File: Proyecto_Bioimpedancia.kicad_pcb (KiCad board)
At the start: 2 copper layers, 100 x 100 mm, 69 parts, among them J1 Jumper, J2 Jumper, J3 Jumper_Calibration, J4 Jumper, J5 Jumper, J6 Jumper, P1 SD_LAPIZ, P10 RS-232, P11 SOURCE_2, P12 RESET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

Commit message: PCB version final
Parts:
- added C14: 0,1uF, Capacitors_SMD:C_0805_HandSoldering, F.Cu at (165.6, 53.1)
- P10: value RS-232 -> UNIVERSAL_PINS; footprint Socket_Strips:Socket_Strip_Straight_1x03_Pitch2.54mm -> Huellas:Universal_Path_80_Pins
- P6: value I2C_1 -> I2C; footprint Socket_Strips:Socket_Strip_Straight_1x02_Pitch2.54mm -> Socket_Strips:Socket_Strip_Straight_2x04_Pitch2.54mm
- P7: value I2C_2 -> CONN_01X04; footprint Socket_Strips:Socket_Strip_Straight_1x02_Pitch2.54mm -> Socket_Strips:Socket_Strip_Straight_1x04_Pitch2.54mm
- moved P10 75.2 mm to (154.5, 124.0), turned to 0 degrees
- moved P7 73.6 mm to (158.0, 48.8), turned to 90 degrees
- moved P12 3.11 mm to (170.8, 48.7)
- moved P6 1.89 mm to (92.3, 87.4), turned to 180 degrees
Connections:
- P6 pad 1: /SDA_R -> /SCL_R
- P6 pad 2: /SCL_R -> /SDA_R
- P7 pad 1: /SDA_R -> /AGND
- P7 pad 2: /SCL_R -> /TXD
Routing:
- net /SDA_R: track 47.7 -> 32.7 mm
- net /SCL_R: track 56.0 -> 43.7 mm, vias 3 -> 2
- net Net-(C14-Pad1): track 0.00 -> 3.03 mm
- net /RXD: track 79.1 -> 76.4 mm
- net /RESET: track 89.0 -> 90.4 mm
- net /AGND: track 172.6 -> 173.6 mm, vias 59 -> 95
- net /SCK: track 21.1 -> 21.9 mm
- net (no net): vias 0 -> 2
- added copper zone on F.Cu, net Net-(C11-Pad2)
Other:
- board text added: "5V"
- board text added: "BIO_OUT1"
- board text added: "BIO_OUT2"
- board text added: "ENC_1"
- board text added: "ENC_2"
- board text added: "GND"
- board text added: "GPIO"
- board text added: "MISO"
- board text added: "MOSI"
- board text added: "RESET"
- board text added: "RX"
- board text added: "RX_V"
- board text added: "SCK"
- board text added: "SCL"
- board text added: "SDA"
- board text added: "TX"
- board text added: "TX_V"
- board text added: "UNIVERSAL_PINS"
- board text added: "V_FUENTE"
- board text added: "~SS"

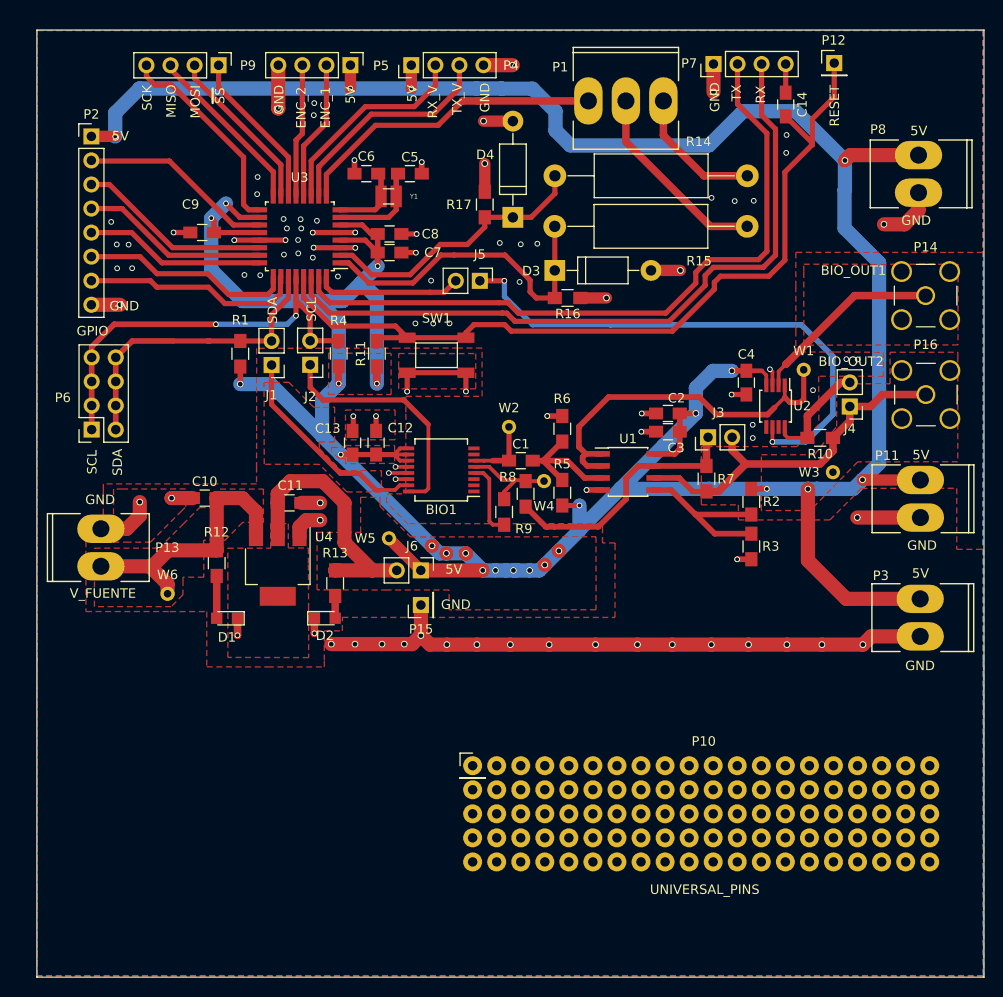
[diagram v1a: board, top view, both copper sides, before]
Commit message: Regleta Universal Añadida
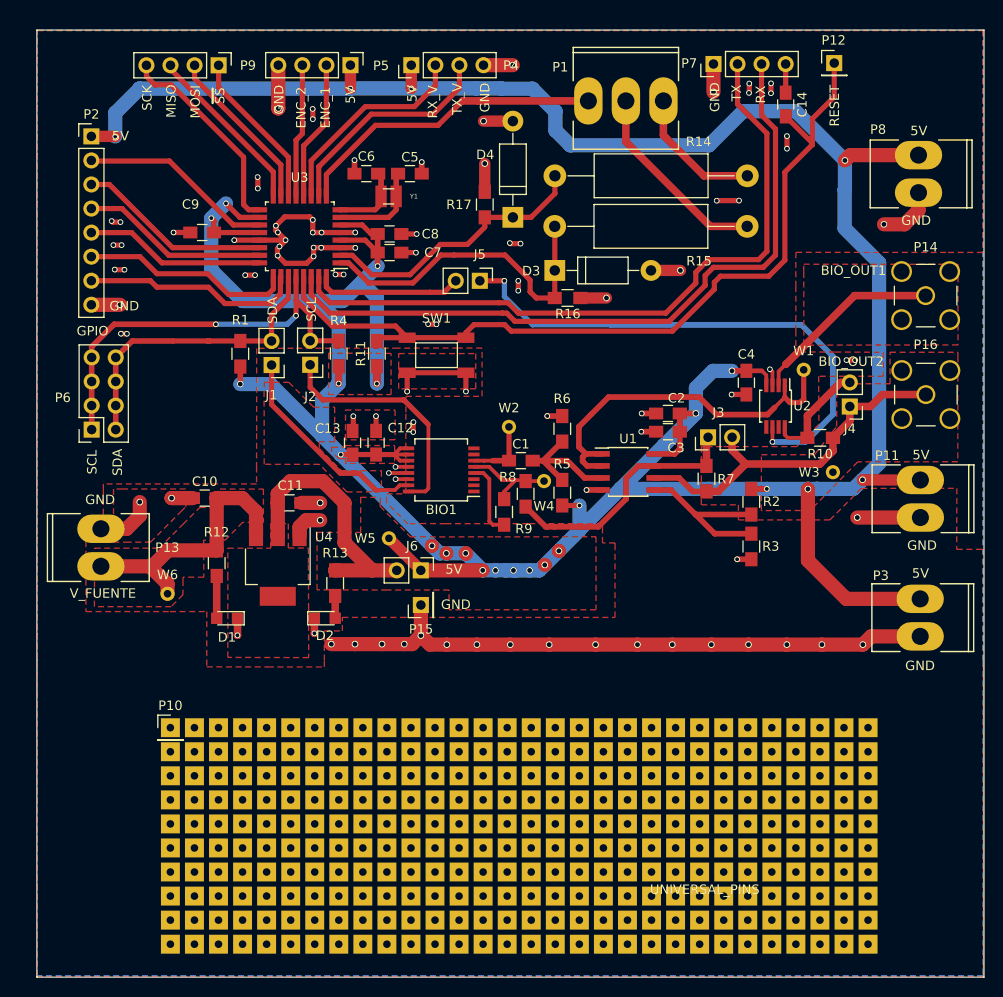
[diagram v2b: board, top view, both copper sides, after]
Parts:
- P10: footprint Huellas:Universal_Path_80_Pins -> Huellas:Universal_Path_300_Pins
- moved P10 54.1 mm to (100.7, 118.9)
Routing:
- net /AGND: track 173.6 -> 207.3 mm, vias 95 -> 100
- net (no net): vias 2 -> 0

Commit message: Gerber generado
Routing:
- net (no net): track 0.00 -> 18.6 mm, vias 0 -> 34
- net /AGND: track 207.3 -> 188.7 mm, vias 100 -> 66

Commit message: Version para placa
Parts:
- added P17: TOR_1, Mounting_Holes:MountingHole_3.2mm_M3_Pad_Via, F.Cu at (91.6, 50.2)
- added P18: TOR_2, Mounting_Holes:MountingHole_3.2mm_M3_Pad_Via, F.Cu at (181.6, 50.2)
- added P19: TOR_3, Mounting_Holes:MountingHole_3.2mm_M3_Pad_Via, F.Cu at (91.6, 140.2)
- added P20: TOR_4, Mounting_Holes:MountingHole_3.2mm_M3_Pad_Via, F.Cu at (181.6, 140.2)
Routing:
- net /AGND: track 188.7 -> 372.8 mm, vias 66 -> 117
- net (no net): track 18.6 -> 0.00 mm, vias 34 -> 0
- net /5V: track 389.5 -> 394.6 mm, vias 26 -> 27
- net /SCL_R: track 43.7 -> 43.2 mm

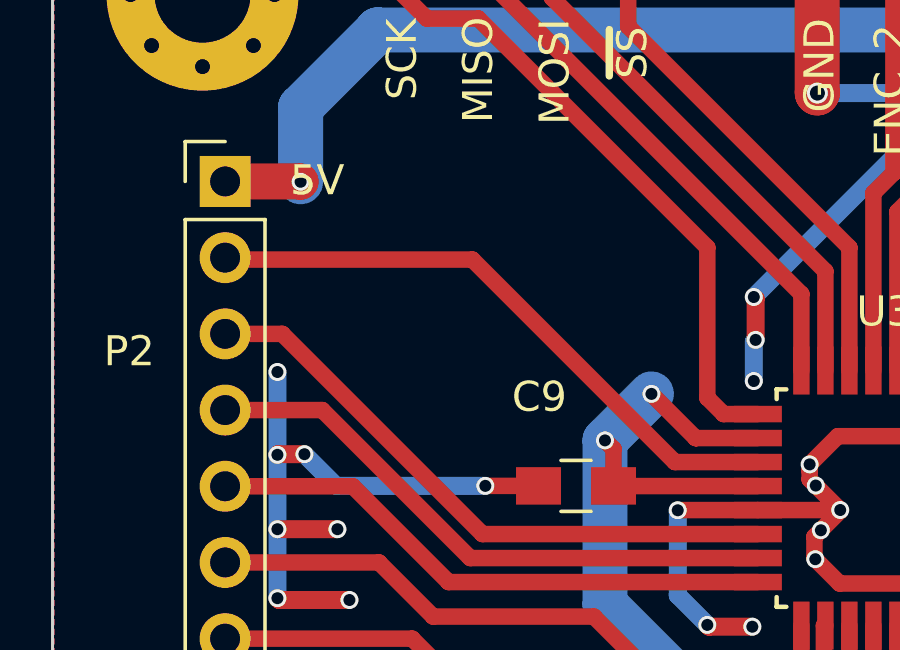
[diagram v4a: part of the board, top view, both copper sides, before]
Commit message: Led Prueba Blink Añadido
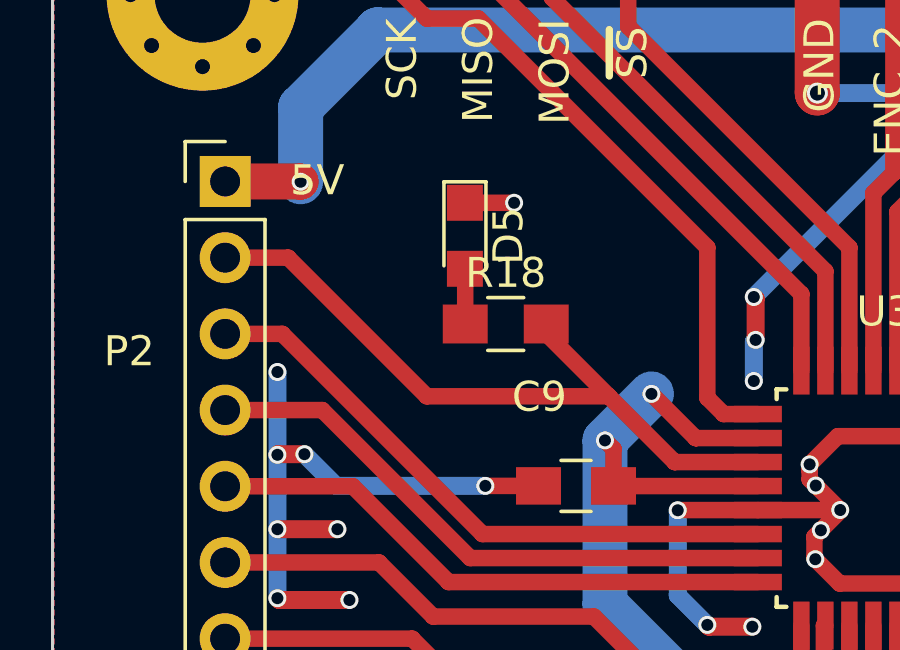
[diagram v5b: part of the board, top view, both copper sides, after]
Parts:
- added D5: Led_Small_Reg, LEDs:LED_0805, F.Cu at (100.3, 58.2)
- added R18: 1K, Resistors_SMD:R_0805_HandSoldering, F.Cu at (101.7, 61.2)
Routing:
- net /REG2_1: track 20.6 -> 23.9 mm
- net Net-(D5-Pad2): track 0.00 -> 1.84 mm
- net /AGND: track 372.8 -> 374.4 mm, vias 117 -> 118
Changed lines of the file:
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@@
 (kicad_pcb (version 4) (host pcbnew 4.0.2-stable)
   (general
-    (links 154)
+    (links 157)
     (no_connects 0)
     (area 86.513199 43.591666 186.613201 145.487)
     (thickness 1.6)
     (drawings 42)
-    (tracks 932)
+    (tracks 940)
     (zones 0)
-    (modules 74)
-    (nets 54)
+    (modules 76)
+    (nets 55)
   )
   (page A4)
@@
   )
   (setup
-    (last_trace_width 0.6)
+    (last_trace_width 0.55)
     (user_trace_width 0.4)
     (user_trace_width 0.5)
@@
   (net 52 "Net-(P19-Pad1)")
   (net 53 "Net-(P20-Pad1)")
+  (net 54 "Net-(D5-Pad2)")
   (net_class Default "Esta es la clase de red por defecto."
     (clearance 0.2)
@@
     (add_net "Net-(D1-Pad2)")
     (add_net "Net-(D2-Pad2)")
+    (add_net "Net-(D5-Pad2)")
     (add_net "Net-(J4-Pad2)")
     (add_net "Net-(J5-Pad2)")
@@
     (pad "" thru_hole circle (at 1.697056 -1.697056) (size 0.8 0.8) (drill 0.5) (layers *.Cu *.Mask))
   )
+  (module LEDs:LED_0805 (layer F.Cu)
+    (at 100.31 58.25 270)
+    (descr "LED 0805 smd package")
+    (tags "LED led 0805 SMD smd SMT smt smdled SMDLED smtled SMTLED")
+    (attr smd)
+    (fp_text reference D5 (at 0 -1.45 270) (layer F.SilkS)
+      (effects (font (size 1 1) (thickness 0.15)))
+    )
+    (fp_text value Led_Small_Reg (at 0 1.55 270) (layer F.Fab)
+      (effects (font (size 1 1) (thickness 0.15)))
+    )
+    (fp_line (start -1.8 -0.7) (end -1.8 0.7) (layer F.SilkS) (width 0.12))
+    (fp_line (start -0.4 -0.4) (end -0.4 0.4) (layer F.Fab) (width 0.1))
+    (fp_line (start -0.4 0) (end 0.2 -0.4) (layer F.Fab) (width 0.1))
+    (fp_line (start 0.2 0.4) (end -0.4 0) (layer F.Fab) (width 0.1))
+    (fp_line (start 0.2 -0.4) (end 0.2 0.4) (layer F.Fab) (width 0.1))
+    (fp_line (start 1 0.6) (end -1 0.6) (layer F.Fab) (width 0.1))
+    (fp_line (start 1 -0.6) (end 1 0.6) (layer F.Fab) (width 0.1))
+    (fp_line (start -1 -0.6) (end 1 -0.6) (layer F.Fab) (width 0.1))
+    (fp_line (start -1 0.6) (end -1 -0.6) (layer F.Fab) (width 0.1))
+    (fp_line (start -1.8 0.7) (end 1 0.7) (layer F.SilkS) (width 0.12))
+    (fp_line (start -1.8 -0.7) (end 1 -0.7) (layer F.SilkS) (width 0.12))
+    (fp_line (start 1.95 -0.85) (end 1.95 0.85) (layer F.CrtYd) (width 0.05))
+    (fp_line (start 1.95 0.85) (end -1.95 0.85) (layer F.CrtYd) (width 0.05))
+    (fp_line (start -1.95 0.85) (end -1.95 -0.85) (layer F.CrtYd) (width 0.05))
+    (fp_line (start -1.95 -0.85) (end 1.95 -0.85) (layer F.CrtYd) (width 0.05))
+    (fp_text user %R (at 0 -1.25 270) (layer F.Fab)
+      (effects (font (size 0.4 0.4) (thickness 0.1)))
+    )
+    (pad 2 smd rect (at 1.1 0 90) (size 1.2 1.2) (layers F.Cu F.Paste F.Mask)
+      (net 54 "Net-(D5-Pad2)"))
+    (pad 1 smd rect (at -1.1 0 90) (size 1.2 1.2) (layers F.Cu F.Paste F.Mask)
+      (net 5 /AGND))
+    (model ${KISYS3DMOD}/LEDs.3dshapes/LED_0805.wrl
+      (at (xyz 0 0 0))
+      (scale (xyz 1 1 1))
+      (rotate (xyz 0 0 180))
+    )
+  )
+  (module Resistors_SMD:R_0805_HandSoldering (layer F.Cu)
+    (at 101.67 61.19)
+    (descr "Resistor SMD 0805, hand soldering")
+    (tags "resistor 0805")
+    (attr smd)
+    (fp_text reference R18 (at 0 -1.7) (layer F.SilkS)
+      (effects (font (size 1 1) (thickness 0.15)))
+    )
+    (fp_text value 1K (at 0 1.75) (layer F.Fab)
+      (effects (font (size 1 1) (thickness 0.15)))
+    )
+    (fp_text user %R (at 0 0) (layer F.Fab)
+      (effects (font (size 0.5 0.5) (thickness 0.075)))
+    )
+    (fp_line (start -1 0.62) (end -1 -0.62) (layer F.Fab) (width 0.1))
+    (fp_line (start 1 0.62) (end -1 0.62) (layer F.Fab) (width 0.1))
+    (fp_line (start 1 -0.62) (end 1 0.62) (layer F.Fab) (width 0.1))
+    (fp_line (start -1 -0.62) (end 1 -0.62) (layer F.Fab) (width 0.1))
+    (fp_line (start 0.6 0.88) (end -0.6 0.88) (layer F.SilkS) (width 0.12))
+    (fp_line (start -0.6 -0.88) (end 0.6 -0.88) (layer F.SilkS) (width 0.12))
+    (fp_line (start -2.35 -0.9) (end 2.35 -0.9) (layer F.CrtYd) (width 0.05))
+    (fp_line (start -2.35 -0.9) (end -2.35 0.9) (layer F.CrtYd) (width 0.05))
+    (fp_line (start 2.35 0.9) (end 2.35 -0.9) (layer F.CrtYd) (width 0.05))
+    (fp_line (start 2.35 0.9) (end -2.35 0.9) (layer F.CrtYd) (width 0.05))
+    (pad 1 smd rect (at -1.35 0) (size 1.5 1.3) (layers F.Cu F.Paste F.Mask)
+      (net 54 "Net-(D5-Pad2)"))
+    (pad 2 smd rect (at 1.35 0) (size 1.5 1.3) (layers F.Cu F.Paste F.Mask)
+      (net 24 /REG2_1))
+    (model ${KISYS3DMOD}/Resistors_SMD.3dshapes/R_0805.wrl
+      (at (xyz 0 0 0))
+      (scale (xyz 1 1 1))
+      (rotate (xyz 0 0 0))
+    )
+  )
   (gr_text UNIVERSAL_PINS (at 136.11 116.37) (layer F.SilkS)
     (effects (font (size 1 1) (thickness 0.25)))
@@
   (segment (start 132.70552 90.67836) (end 133.76438 90.67836) (width 0.4) (layer F.Cu) (net 3))
   (segment (start 133.76438 90.67836) (end 133.7691 90.68308) (width 0.4) (layer F.Cu) (net 3))
+  (segment (start 100.31 57.15) (end 101.95 57.15) (width 0.55) (layer F.Cu) (net 5))
+  (via (at 101.95 57.15) (size 0.6) (drill 0.4) (layers F.Cu B.Cu) (net 5))
   (segment (start 121.31 76.32) (end 120.86 76.77) (width 0.6) (layer B.Cu) (net 5))
   (via (at 119.87 77.56) (size 0.6) (drill 0.4) (layers F.Cu B.Cu) (net 5))
@@
   (segment (start 119.4749 69.7925) (end 121.59996 71.91756) (width 0.55) (layer F.Cu) (net 23))
   (segment (start 121.59996 71.91756) (end 121.63044 71.94804) (width 0.55) (layer F.Cu) (net 23))
+  (segment (start 103.02 61.19) (end 103.02 61.51) (width 0.55) (layer F.Cu) (net 24))
+  (segment (start 103.02 61.51) (end 105.11 63.6) (width 0.55) (layer F.Cu) (net 24))
+  (segment (start 107.3088 65.7925) (end 107.3025 65.7925) (width 0.55) (layer F.Cu) (net 24))
   (segment (start 110.0754 65.7925) (end 107.3088 65.7925) (width 0.55) (layer F.Cu) (net 24))
-  (segment (start 100.5586 59.0423) (end 92.3798 59.0423) (width 0.55) (layer F.Cu) (net 24))
-  (segment (start 107.3088 65.7925) (end 100.5586 59.0423) (width 0.55) (layer F.Cu) (net 24))
-  (segment (start 92.3798 59.0423) (end 92.3163 58.9788) (width 0.55) (layer F.Cu) (net 24))
+  (segment (start 94.4188 58.9788) (end 92.3163 58.9788) (width 0.55) (layer F.Cu) (net 24))
+  (segment (start 99.04 63.6) (end 94.4188 58.9788) (width 0.55) (layer F.Cu) (net 24))
+  (segment (start 105.11 63.6) (end 99.04 63.6) (width 0.55) (layer F.Cu) (net 24))
+  (segment (start 107.3025 65.7925) (end 105.11 63.6) (width 0.55) (layer F.Cu) (net 24))
   (segment (start 110.0754 68.1925) (end 100.8953 68.1925) (width 0.55) (layer F.Cu) (net 25))
   (segment (start 94.2216 61.5188) (end 92.3163 61.5188) (width 0.55) (layer F.Cu) (net 25))
@@
   (segment (start 165.625 51.825) (end 165.625 48.805) (width 0.55) (layer F.Cu) (net 48))
   (segment (start 165.625 48.805) (end 165.62 48.8) (width 0.55) (layer F.Cu) (net 48))
+  (segment (start 100.32 61.19) (end 100.32 59.36) (width 0.55) (layer F.Cu) (net 54))
+  (segment (start 100.32 59.36) (end 100.31 59.35) (width 0.55) (layer F.Cu) (net 54))
   (zone (net 5) (net_name /AGND) (layer B.Cu) (hatch edge 0.508)
     (connect_pads (clearance 0.508))
